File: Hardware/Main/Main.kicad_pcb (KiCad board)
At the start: 4 copper layers, 50 x 72 mm, 56 parts, among them J1 POWERBOARD, J2 ProgHeader, SW1 SW_Push, SW2 SW_Push, SW3 SW_Push, SW4 RotaryEncoder_Switch, SW5 SW_Push, U1 TFT_ST7789, U2 ESP32-WROOM-32D, U3 TCA4311a

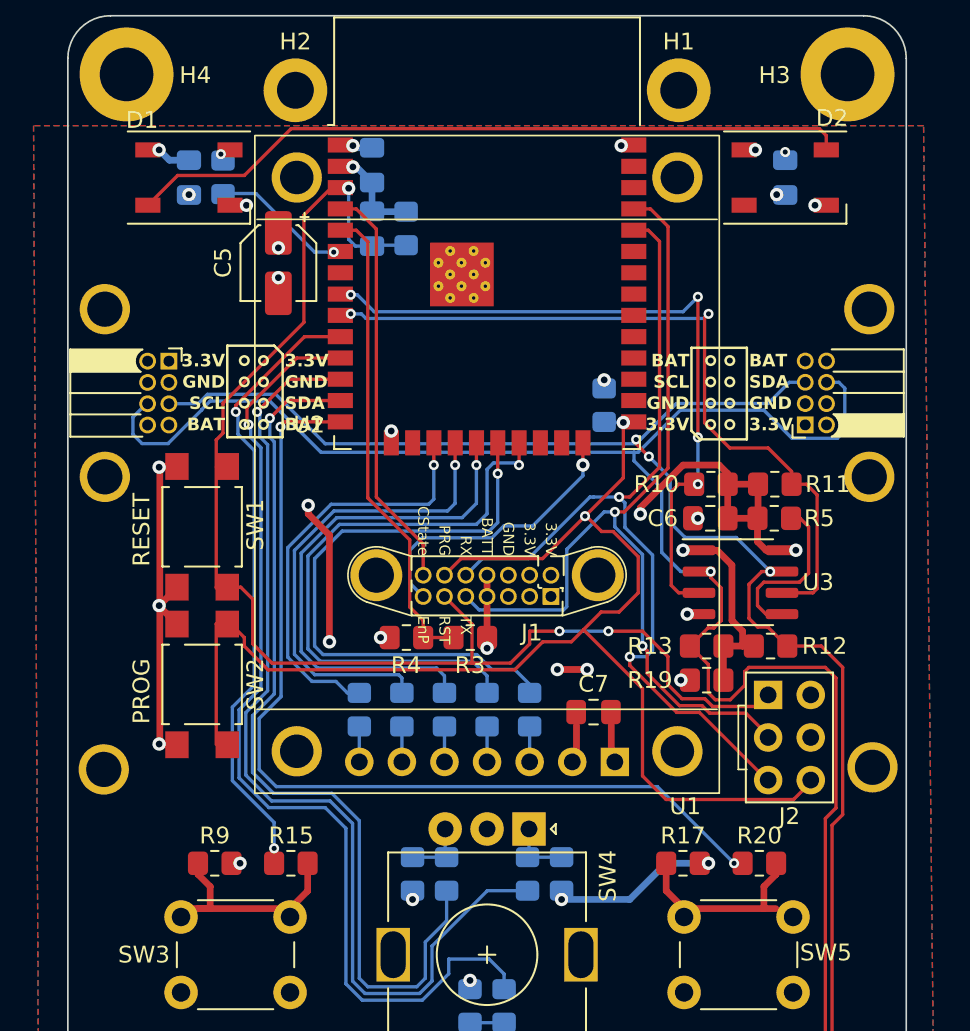
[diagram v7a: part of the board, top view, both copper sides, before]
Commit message: Add extra mountingscrew to side peripherals
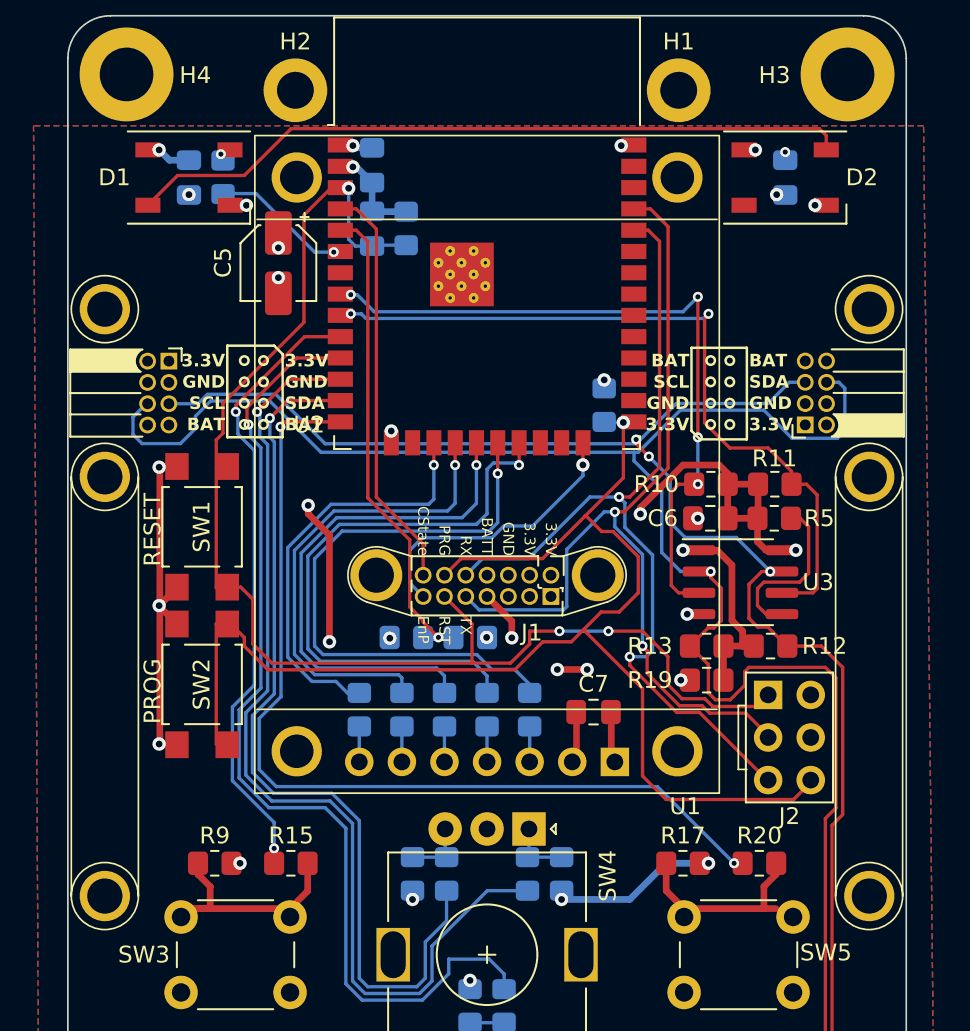
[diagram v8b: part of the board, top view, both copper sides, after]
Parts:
- removed ? (x2): , 
- Per2: footprint Connectors:PeripheralMaster -> Connectors:PeripheralMaster_Right
- Per3: footprint Connectors:PeripheralMaster -> Connectors:PeripheralMaster_Left
- R3, R4: moved to B.Cu
- moved R3 3.81 mm to (-4.81, -34.9), turned to 180 degrees
- moved R4 3.81 mm to (-1.00, -34.9), turned to 180 degrees
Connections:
- Per1 pad 9: (no net) -> GND
- Per2 pad 9: (no net) -> GND
- Per3 pad 9: (no net) -> GND
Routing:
- net GND: track 324.6 -> 367.2 mm
- net +BATT: track 105.5 -> 108.5 mm, vias 3 -> 4
- net BatSense: track 28.7 -> 29.1 mm, vias 0 -> 1
- net ID0Prog: vias 2 -> 1
